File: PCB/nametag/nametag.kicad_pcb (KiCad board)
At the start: 4 copper layers, 61 x 31 mm, 55 parts, among them J1 USB_C_Receptacle_USB2.0_14P, J3 Conn_02x03_Odd_Even, Q1 NXV55UN, U1 MIC550x, U2 AVR64DU32, U3 23K640, U4 MCP9700x-ETT, U5 SN74LV1T125DBV, U6 SN74LV1T125DBV

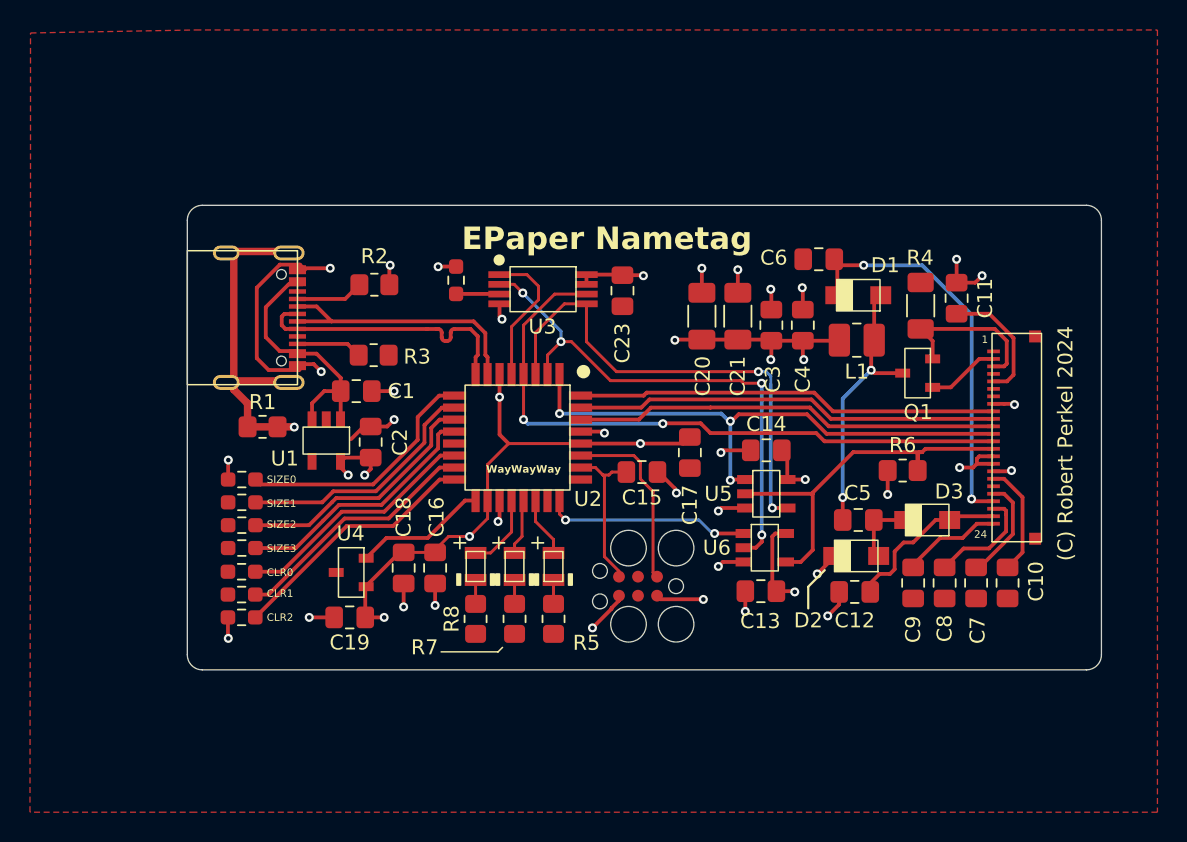
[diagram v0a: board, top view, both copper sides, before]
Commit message: Created common SPI library
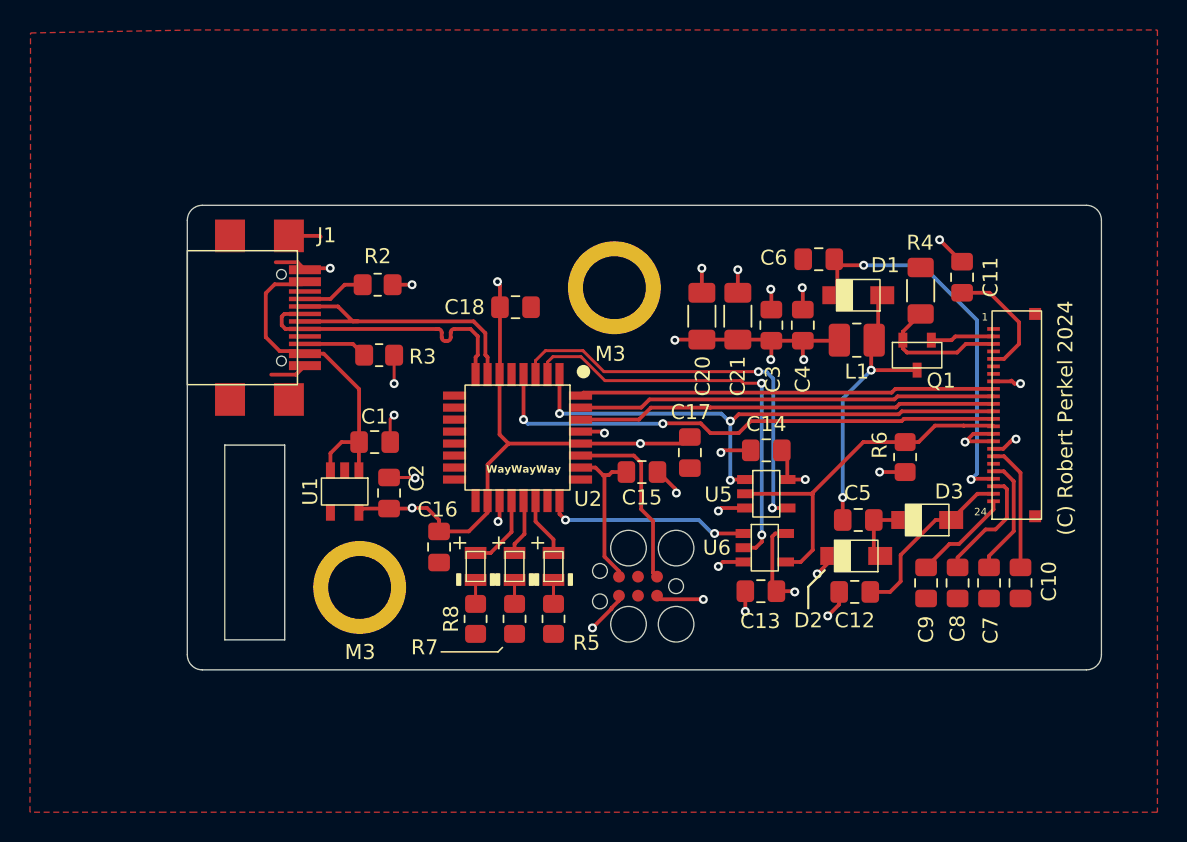
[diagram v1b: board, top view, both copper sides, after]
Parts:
- removed C19, C23: 0.1uF, 16V, Capacitor_SMD:C_0805_2012Metric_Pad1.18x1.45mm_HandSolder
- removed CLR0, CLR1, CLR2, R9, SIZE0, SIZE1, SIZE2, SIZE3: 0, Resistor_SMD:R_0603_1608Metric_Pad0.98x0.95mm_HandSolder
- removed R1: 0, Resistor_SMD:R_0805_2012Metric_Pad1.20x1.40mm_HandSolder
- removed U3: 23K640, Microchip:TSSOP-8 (ST)
- removed U4: MCP9700x-ETT, StandardPackages_Custom:SOT23-3
- added REF**: 24939, nametag:24939, F.Cu at (181.0, 115.0)
- added REF**: 24939, nametag:24939, F.Cu at (198.0, 95.0)
- J1: value USB_C_Receptacle_USB2.0_14P -> GSB1C41110SSHR; footprint nametag:12402012E212A -> nametag:GSB1C41110SSHR
- moved C18 18.9 mm to (191.4, 96.3), turned to 0 degrees
- moved C2 3.61 mm to (183.0, 108.7)
- moved C1 3.61 mm to (182.0, 105.3)
- moved U1 3.61 mm to (180.0, 108.6)
- moved J2 1.50 mm to (223.5, 103.5)
- moved C11 1.45 mm to (221.2, 94.3)
- moved C16 1.42 mm to (186.3, 112.3)
- moved Q1 1.20 mm to (218.2, 99.5), turned to 0 degrees
- moved R4 1.00 mm to (218.4, 95.2)
- moved R6 0.91 mm to (217.4, 106.3), turned to -90 degrees
- moved C7 0.86 mm to (223.0, 114.7)
- moved C8 0.86 mm to (220.9, 114.7)
- moved C9 0.86 mm to (218.8, 114.7)
- moved C10 0.86 mm to (225.1, 114.7)
- moved R3 0.36 mm to (182.3, 99.5)
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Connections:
- net ~{DISP_MISO_EN} renamed ~{DISP_MOSI_EN}
- U2 pad 10: Net-(U2-PD0) -> unconnected-(U2-PD0-Pad10)
- U2 pad 11: Net-(U2-PD1) -> unconnected-(U2-PD1-Pad11)
- U2 pad 12: Net-(U2-PD2) -> unconnected-(U2-PD2-Pad12)
- U2 pad 14: Net-(U2-PD4) -> unconnected-(U2-PD4-Pad14)
- U2 pad 15: Net-(U2-PD5) -> unconnected-(U2-PD5-Pad15)
- U2 pad 16: Net-(U2-PD6) -> unconnected-(U2-PD6-Pad16)
- U2 pad 17: TEMP -> unconnected-(U2-PD7-Pad17)
- U2 pad 5: ~{FLASH_CS} -> unconnected-(U2-PA7-Pad5)
- U2 pad 9: Net-(U2-PC3) -> unconnected-(U2-PC3-Pad9)
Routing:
- net GND: track 86.1 -> 47.7 mm, vias 31 -> 23
- net Net-(U2-PD6): track 17.1 -> 0.00 mm
- net Net-(U2-PD2): track 17.0 -> 0.00 mm
- net Net-(U2-PD1): track 16.9 -> 0.00 mm
- net Net-(U2-PD5): track 16.8 -> 0.00 mm
- net Net-(U2-PC3): track 16.8 -> 0.00 mm
- net Net-(U2-PD0): track 16.6 -> 0.00 mm
- net Net-(U2-PD4): track 16.5 -> 0.00 mm
- net ~{FLASH_CS}: track 9.57 -> 0.00 mm
- net +3.3V: track 76.4 -> 67.3 mm, vias 15 -> 10
- net TEMP: track 8.97 -> 0.00 mm
- net SCLK: track 43.3 -> 35.2 mm
- net MOSI: track 35.1 -> 27.9 mm, vias 4 -> 2
- net MISO: track 32.6 -> 27.5 mm
- net +5V: track 17.3 -> 21.3 mm
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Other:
- outline, holes or cut-outs redrawn
- board text added: "M3"
- board text removed: "${TITLE}"

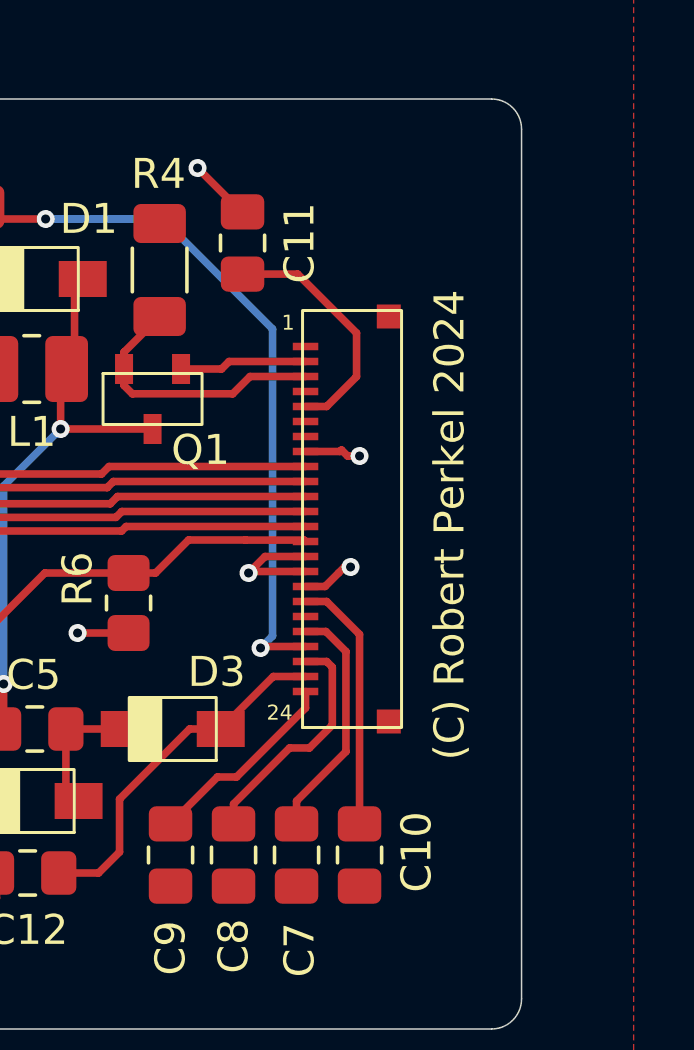
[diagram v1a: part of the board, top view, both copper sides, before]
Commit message: README edits. Added renders and BOM
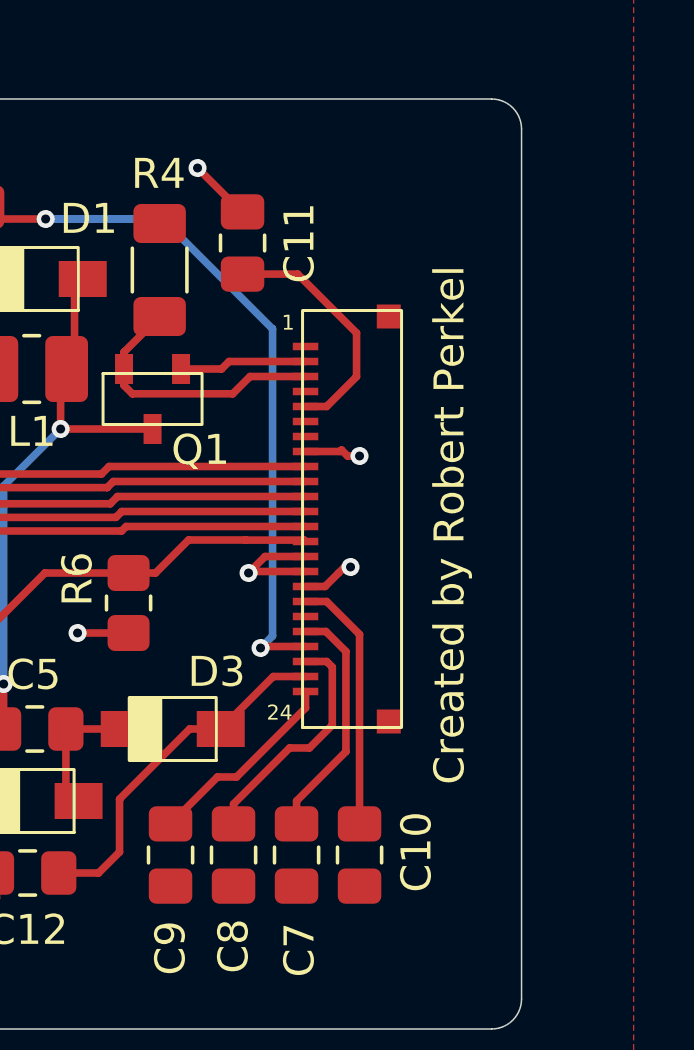
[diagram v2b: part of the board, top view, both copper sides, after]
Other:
- board text added: "Created by Robert Perkel"
- board text removed: "(C) Robert Perkel 2024"
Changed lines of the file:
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@@
 	(title_block
 		(title "EPaper Nametag")
-		(date "2024-06-09")
-		(rev "A2")
+		(date "2024-08-09")
+		(rev "A3")
+		(company "Created by Robert Perkel")
 	)
 	(layers
@@
 		)
 	)
-	(gr_text "(C) Robert Perkel 2024"
+	(gr_text "Created by Robert Perkel"
 		(at 228.1 103.7 90)
 		(layer "F.SilkS")
